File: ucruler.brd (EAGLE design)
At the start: 200 x 32 mm, 61 parts

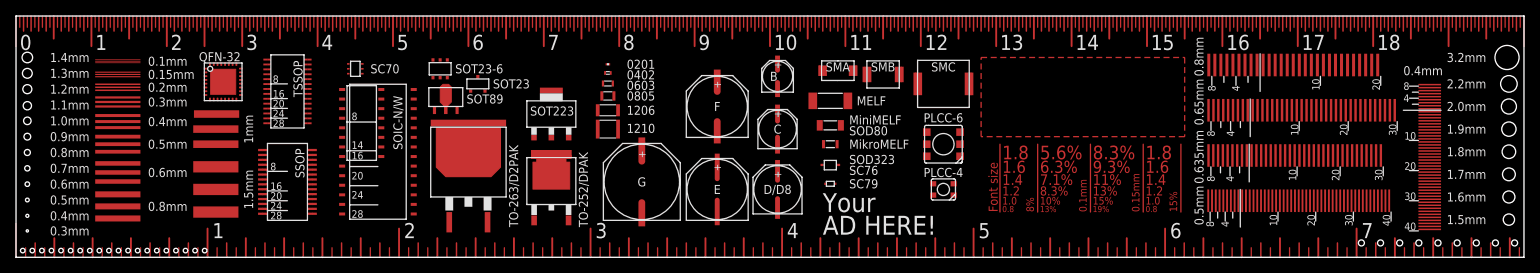
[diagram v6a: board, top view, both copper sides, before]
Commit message: table for alu ecap sizes
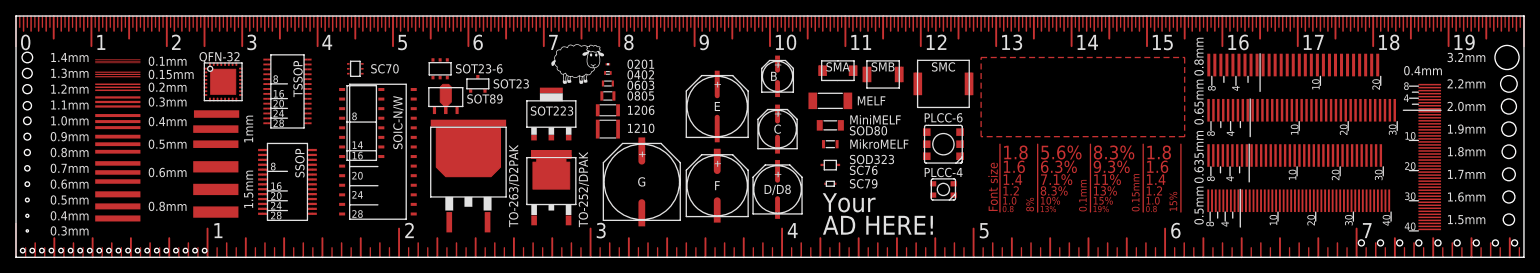
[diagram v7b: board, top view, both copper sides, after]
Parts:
- added E$62: (no value), grafiken:SCHAF-7
- added E$63: (no value), ucruler:SILK-TABLE-ECAP
- moved E$54 11.0 mm to (93.0, 20.0)
- moved E$55 10.5 mm to (93.0, 9.50)
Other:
- board text added: "19"
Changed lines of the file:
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@@
 <layer number="19" name="Unrouted" color="6" fill="1" visible="yes" active="yes"/>
 <layer number="20" name="Dimension" color="15" fill="1" visible="yes" active="yes"/>
-<layer number="21" name="tPlace" color="7" fill="1" visible="yes" active="yes"/>
-<layer number="22" name="bPlace" color="7" fill="1" visible="no" active="yes"/>
+<layer number="21" name="tPlace" color="7" fill="1" visible="no" active="yes"/>
+<layer number="22" name="bPlace" color="7" fill="1" visible="yes" active="yes"/>
 <layer number="23" name="tOrigins" color="15" fill="1" visible="yes" active="yes"/>
 <layer number="24" name="bOrigins" color="15" fill="1" visible="no" active="yes"/>
@@
 <layer number="97" name="Info" color="7" fill="1" visible="no" active="no"/>
 <layer number="98" name="Guide" color="6" fill="1" visible="no" active="no"/>
+<layer number="200" name="200bmp" color="1" fill="10" visible="yes" active="yes"/>
+<layer number="201" name="201bmp" color="2" fill="10" visible="no" active="yes"/>
+<layer number="202" name="202bmp" color="3" fill="10" visible="no" active="yes"/>
+<layer number="203" name="203bmp" color="4" fill="10" visible="no" active="yes"/>
 </layers>
 <board>
@@
 <text x="17.5" y="26" size="1.2" layer="21" ratio="13" align="center-left">0.1mm</text>
 <text x="83" y="10" size="1.2" layer="21" ratio="13" distance="20" align="center">G</text>
-<text x="93" y="9" size="1.2" layer="21" ratio="13" distance="20" align="center">E</text>
-<text x="93" y="20" size="1.2" layer="21" ratio="13" distance="20" align="center">F</text>
+<text x="93" y="20" size="1.2" layer="21" ratio="13" distance="20" align="center">E</text>
+<text x="93" y="9.5" size="1.2" layer="21" ratio="13" distance="20" align="center">F</text>
 <text x="101" y="9" size="1.2" layer="21" ratio="13" distance="20" align="center">D/D8</text>
 <text x="101" y="17" size="1.2" layer="21" ratio="13" distance="20" align="center">C</text>
@@
 <hole x="25.019" y="0.889" drill="0.6"/>
 <text x="4.5" y="3.5" size="1.2" layer="21" ratio="13" align="center-left">0.3mm</text>
+<text x="190.5" y="29.5" size="2" layer="21" font="fixed" align="top-left">19</text>
 </plain>
 <attributes>
@@
 <element name="E$52" library="ucruler" package="PACK-ECAP-5.3" value="" x="101" y="17"/>
 <element name="E$53" library="ucruler" package="PACK-ECAP-6.6" value="" x="101" y="9"/>
-<element name="E$54" library="ucruler" package="PACK-ECAP-8.3-E" value="" x="93" y="9"/>
-<element name="E$55" library="ucruler" package="PACK-ECAP-8.3-F" value="" x="93" y="20"/>
+<element name="E$54" library="ucruler" package="PACK-ECAP-8.3-E" value="" x="93" y="20"/>
+<element name="E$55" library="ucruler" package="PACK-ECAP-8.3-F" value="" x="93" y="9.5"/>
 <element name="E$56" library="ucruler" package="PACK-ECAP-10.3" value="" x="83" y="10"/>
 <element name="E$57" library="ucruler" package="PACK-SSOP" value="" x="36" y="10"/>
@@
 <element name="E$60" library="ucruler" package="COPPER-FONT" value="" x="129" y="6"/>
 <element name="E$61" library="ucruler" package="SILK-FONT-INV" value="" x="131" y="28.5" rot="MR270"/>
+<element name="E$62" library="grafiken" package="SCHAF-7" value="" x="71" y="23"/>
+<element name="E$63" library="ucruler" package="SILK-TABLE-ECAP" value="" x="72.5" y="29" rot="MR0"/>
 </elements>
 <signals>

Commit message: corrected font rotation of bottom silk print table
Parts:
- removed E$61: (no value), ucruler:SILK-FONT-INV
- added E$64: (no value), ucruler:SILK-FONT-INV-R
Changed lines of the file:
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@@
 <grid distance="1" unitdist="mm" unit="mm" style="lines" multiple="1" display="yes" altdistance="0.5" altunitdist="mm" altunit="mm"/>
 <layers>
-<layer number="1" name="Top" color="4" fill="1" visible="yes" active="yes"/>
+<layer number="1" name="Top" color="4" fill="1" visible="no" active="yes"/>
 <layer number="2" name="Route2" color="1" fill="3" visible="no" active="no"/>
 <layer number="3" name="Route3" color="4" fill="3" visible="no" active="no"/>
@@
 <layer number="21" name="tPlace" color="7" fill="1" visible="no" active="yes"/>
 <layer number="22" name="bPlace" color="7" fill="1" visible="yes" active="yes"/>
-<layer number="23" name="tOrigins" color="15" fill="1" visible="yes" active="yes"/>
-<layer number="24" name="bOrigins" color="15" fill="1" visible="no" active="yes"/>
-<layer number="25" name="tNames" color="7" fill="1" visible="yes" active="yes"/>
-<layer number="26" name="bNames" color="7" fill="1" visible="no" active="yes"/>
+<layer number="23" name="tOrigins" color="15" fill="1" visible="no" active="yes"/>
+<layer number="24" name="bOrigins" color="15" fill="1" visible="yes" active="yes"/>
+<layer number="25" name="tNames" color="7" fill="1" visible="no" active="yes"/>
+<layer number="26" name="bNames" color="7" fill="1" visible="yes" active="yes"/>
 <layer number="27" name="tValues" color="7" fill="1" visible="no" active="yes"/>
 <layer number="28" name="bValues" color="7" fill="1" visible="no" active="yes"/>
-<layer number="29" name="tStop" color="7" fill="3" visible="yes" active="yes"/>
+<layer number="29" name="tStop" color="7" fill="3" visible="no" active="yes"/>
 <layer number="30" name="bStop" color="7" fill="6" visible="no" active="yes"/>
 <layer number="31" name="tCream" color="7" fill="4" visible="no" active="yes"/>
@@
 <layer number="37" name="tTest" color="7" fill="1" visible="no" active="yes"/>
 <layer number="38" name="bTest" color="7" fill="1" visible="no" active="yes"/>
-<layer number="39" name="tKeepout" color="4" fill="11" visible="yes" active="yes"/>
+<layer number="39" name="tKeepout" color="4" fill="11" visible="no" active="yes"/>
 <layer number="40" name="bKeepout" color="1" fill="11" visible="no" active="yes"/>
-<layer number="41" name="tRestrict" color="4" fill="10" visible="yes" active="yes"/>
+<layer number="41" name="tRestrict" color="4" fill="10" visible="no" active="yes"/>
 <layer number="42" name="bRestrict" color="1" fill="10" visible="no" active="yes"/>
 <layer number="43" name="vRestrict" color="2" fill="10" visible="yes" active="yes"/>
@@
 <hole x="193.675" y="1.905" drill="0.8"/>
 <hole x="191.135" y="1.905" drill="0.8"/>
-<text x="43.41" y="25.73" size="1.2" layer="22" rot="MR0" align="top-left">VIA Current
+<text x="41.41" y="28.73" size="1.2" layer="22" rot="MR0" align="top-left">VIA Current
 [mm] [A]
 0,2  1
@@
 <element name="E$8" library="ucruler" package="COPPER-FONT-INV" value="" x="129" y="17"/>
 <element name="E$60" library="ucruler" package="COPPER-FONT" value="" x="129" y="6"/>
-<element name="E$61" library="ucruler" package="SILK-FONT-INV" value="" x="131" y="28.5" rot="MR270"/>
 <element name="E$62" library="grafiken" package="SCHAF-7" value="" x="71" y="23"/>
 <element name="E$63" library="ucruler" package="SILK-TABLE-ECAP" value="" x="72.5" y="29" rot="MR0"/>
+<element name="E$64" library="ucruler" package="SILK-FONT-INV-R" value="" x="131" y="28.5" rot="MR0"/>
 </elements>
 <signals>
